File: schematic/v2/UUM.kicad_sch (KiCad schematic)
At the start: 9 parts, among them U3 NUCLEO-F303RE

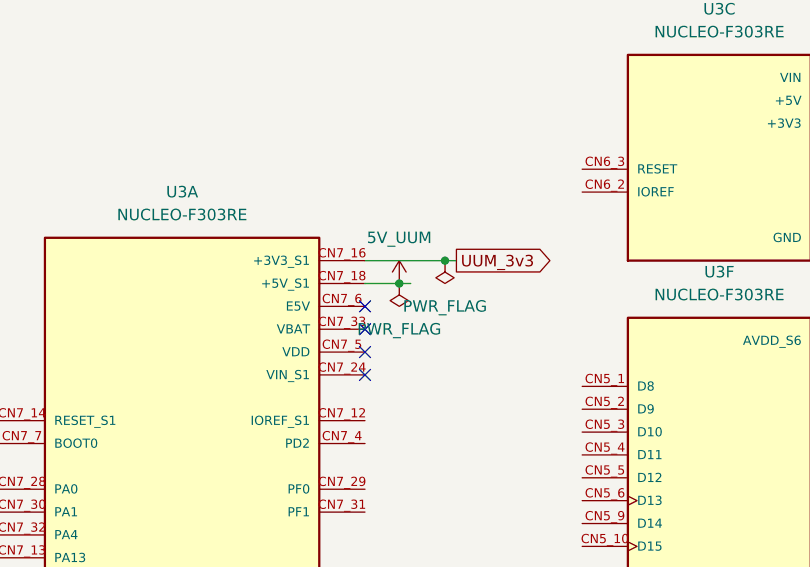
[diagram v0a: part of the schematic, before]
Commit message: need to update PCB and new traces
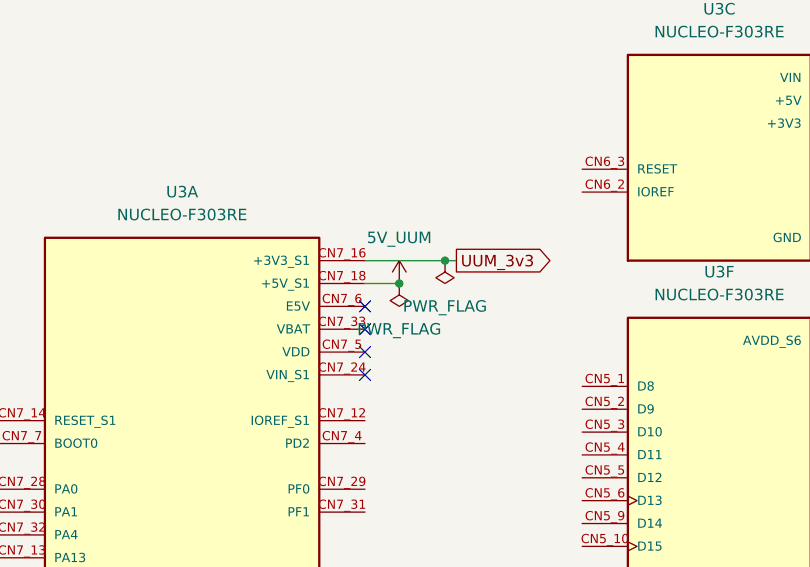
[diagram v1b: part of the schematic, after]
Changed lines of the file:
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@@
-	(wire
-		(pts
-			(xy 215.9 46.99) (xy 217.17 46.99)
-		)
-		(stroke
-			(width 0)
-			(type default)
-		)
-	)
 	(wire
 		(pts

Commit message: time to start routing?
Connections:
- net UUM_VDD is gone; now on net 5V_UUM: R45.2
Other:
- removed sheet UUM_debug
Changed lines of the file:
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@@
 	)
 	(junction
-		(at 220.98 44.45)
+		(at 220.98 40.64)
 		(diameter 0)
 		(color 0 0 0 0)
@@
 	(wire
 		(pts
-			(xy 104.14 76.2) (xy 87.63 76.2)
+			(xy 157.48 115.57) (xy 171.45 115.57)
 		)
 		(stroke
@@
 	(wire
 		(pts
-			(xy 157.48 115.57) (xy 171.45 115.57)
+			(xy 104.14 104.14) (xy 87.63 104.14)
 		)
 		(stroke
@@
 	(wire
 		(pts
-			(xy 104.14 104.14) (xy 87.63 104.14)
+			(xy 127 140.97) (xy 130.81 140.97)
 		)
 		(stroke
@@
 	(wire
 		(pts
-			(xy 212.09 44.45) (xy 220.98 44.45)
+			(xy 137.16 157.48) (xy 151.13 157.48)
 		)
 		(stroke
@@
 	(wire
 		(pts
-			(xy 127 140.97) (xy 130.81 140.97)
+			(xy 107.95 69.85) (xy 124.46 69.85)
 		)
 		(stroke
@@
 	(wire
 		(pts
-			(xy 137.16 157.48) (xy 151.13 157.48)
+			(xy 157.48 157.48) (xy 171.45 157.48)
 		)
 		(stroke
@@
 	(wire
 		(pts
-			(xy 107.95 69.85) (xy 124.46 69.85)
+			(xy 107.95 72.39) (xy 124.46 72.39)
 		)
 		(stroke
@@
 	(wire
 		(pts
-			(xy 157.48 157.48) (xy 171.45 157.48)
+			(xy 187.96 140.97) (xy 191.77 140.97)
 		)
 		(stroke
@@
 	(wire
 		(pts
-			(xy 107.95 72.39) (xy 124.46 72.39)
+			(xy 104.14 111.76) (xy 87.63 111.76)
 		)
 		(stroke
@@
 	(wire
 		(pts
-			(xy 187.96 140.97) (xy 191.77 140.97)
+			(xy 171.45 148.59) (xy 171.45 149.86)
 		)
 		(stroke
@@
 	(wire
 		(pts
-			(xy 104.14 111.76) (xy 87.63 111.76)
+			(xy 212.09 40.64) (xy 220.98 40.64)
 		)
 		(stroke
@@
 	(wire
 		(pts
-			(xy 171.45 148.59) (xy 171.45 149.86)
+			(xy 104.14 114.3) (xy 87.63 114.3)
 		)
 		(stroke
@@
 	(wire
 		(pts
-			(xy 104.14 114.3) (xy 87.63 114.3)
+			(xy 160.02 123.19) (xy 162.56 123.19)
 		)
 		(stroke
@@
 	(wire
 		(pts
-			(xy 160.02 123.19) (xy 162.56 123.19)
+			(xy 212.09 40.64) (xy 212.09 44.45)
 		)
 		(stroke
@@
 	(wire
 		(pts
-			(xy 107.95 57.15) (xy 124.46 57.15)
+			(xy 121.92 57.15) (xy 124.46 57.15)
 		)
 		(stroke
@@
 	(wire
 		(pts
-			(xy 220.98 44.45) (xy 222.25 44.45)
+			(xy 220.98 40.64) (xy 222.25 40.64)
 		)
 		(stroke
@@
 	(wire
 		(pts
-			(xy 104.14 78.74) (xy 87.63 78.74)
+			(xy 104.14 101.6) (xy 87.63 101.6)
 		)
 		(stroke
@@
 	(wire
 		(pts
-			(xy 104.14 101.6) (xy 87.63 101.6)
+			(xy 107.95 62.23) (xy 124.46 62.23)
 		)
 		(stroke
@@
 	(wire
 		(pts
-			(xy 107.95 62.23) (xy 124.46 62.23)
+			(xy 215.9 46.99) (xy 218.44 46.99)
 		)
 		(stroke
@@
 	(wire
 		(pts
-			(xy 107.95 59.69) (xy 124.46 59.69)
+			(xy 121.92 59.69) (xy 124.46 59.69)
 		)
 		(stroke
@@
 		)
 	)
-	(label "UUM_DBG_RX"
-		(at 107.95 59.69 0)
-		(effects
-			(font
-				(size 1.27 1.27)
-			)
-			(justify left bottom)
-		)
-	)
 	(label "UUM_SPI1_MISO"
 		(at 104.14 104.14 180)
@@
 		)
 	)
-	(label "UUM_DBG_TX"
-		(at 107.95 57.15 0)
-		(effects
-			(font
-				(size 1.27 1.27)
-			)
-			(justify left bottom)
-		)
-	)
 	(label "UUM_SPI1_MOSI"
 		(at 107.95 67.31 0)
@@
 		)
 	)
-	(label "UUM_DBG_TX"
-		(at 104.14 78.74 180)
-		(effects
-			(font
-				(size 1.27 1.27)
-			)
-			(justify right bottom)
-		)
-	)
-	(label "UUM_DBG_RX"
-		(at 104.14 76.2 180)
-		(effects
-			(font
-				(size 1.27 1.27)
-			)
-			(justify right bottom)
-		)
-	)
 	(global_label "UUM_VDD"
 		(shape input)
@@
 	(global_label "UUM_3v3"
 		(shape output)
-		(at 222.25 44.45 0)
+		(at 222.25 40.64 0)
 		(fields_autoplaced yes)
 		(effects
@@
 		)
 		(property "Intersheetrefs" "${INTERSHEET_REFS}"
-			(at 233.7018 44.45 0)
+			(at 233.7018 40.64 0)
 			(effects
 				(font
@@
 		)
 	)
+	(hierarchical_label "UUM_DBG_TX"
+		(shape output)
+		(at 121.92 57.15 180)
+		(effects
+			(font
+				(size 1.27 1.27)
+			)
+			(justify right)
+		)
+	)
+	(hierarchical_label "UUM_VDD"
+		(shape output)
+		(at 218.44 46.99 0)
+		(effects
+			(font
+				(size 1.27 1.27)
+			)
+			(justify left)
+		)
+	)
+	(hierarchical_label "UUM_DBG_RX"
+		(shape input)
+		(at 121.92 59.69 180)
+		(effects
+			(font
+				(size 1.27 1.27)
+			)
+			(justify right)
+		)
+	)
 	(symbol
 		(lib_id "Device:R")
@@
 	(symbol
 		(lib_id "power:PWR_FLAG")
-		(at 220.98 44.45 180)
+		(at 220.98 40.64 180)
 		(unit 1)
 		(exclude_from_sim no)
@@
 		(fields_autoplaced yes)
 		(property "Reference" "#FLG07"
-			(at 220.98 46.355 0)
+			(at 220.98 42.545 0)
 			(effects
 				(font
@@
 		)
 		(property "Value" "PWR_FLAG"
-			(at 220.98 49.53 0)
+			(at 220.98 45.72 0)
 			(effects
 				(font
@@
 		)
 		(property "Footprint" ""
-			(at 220.98 44.45 0)
+			(at 220.98 40.64 0)
 			(effects
 				(font
@@
 		)
 		(property "Datasheet" "~"
-			(at 220.98 44.45 0)
+			(at 220.98 40.64 0)
 			(effects
 				(font
@@
 		)
 		(property "Description" "Special symbol for telling ERC where power comes from"
-			(at 220.98 44.45 0)
+			(at 220.98 40.64 0)
 			(effects
 				(font
@@
 				)
 			)
-		)
-	)
-	(sheet
-		(at 71.12 72.39)
-		(size 16.51 10.16)
-		(exclude_from_sim no)
-		(in_bom yes)
-		(on_board yes)
-		(dnp no)
-		(fields_autoplaced yes)
-		(stroke
-			(width 0.1524)
-			(type solid)
-		)
-		(fill
-			(color 0 0 0 0.0000)
-		)
-		(property "Sheetname" "UUM_debug"
-			(at 71.12 71.6784 0)
-			(effects
-				(font
-					(size 1.27 1.27)
-				)
-				(justify left bottom)
-			)
-		)
-		(property "Sheetfile" "UUM_debug.kicad_sch"
-			(at 71.12 83.1346 0)
-			(effects
-				(font
-					(size 1.27 1.27)
-				)
-				(justify left top)
-			)
-		)
-		(pin "UUM_DBG_RX" input
-			(at 87.63 78.74 0)
-			(effects
-				(font
-					(size 1.27 1.27)
-				)
-				(justify right)
-			)
-		)
-		(pin "UUM_DBG_TX" input
-			(at 87.63 76.2 0)
-			(effects
-				(font
-					(size 1.27 1.27)
-				)
-				(justify right)
-			)
-		)
-		(instances
-			(project "signalmesh"
-				(path "/fe7b15e9-f0ed-4338-9f03-dd7651dace13/e0c3e94a-d1d6-4c70-a171-e825d34fc315"
-					(page "16")
-				)
-			)
